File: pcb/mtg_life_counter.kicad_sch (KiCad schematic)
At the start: 41 parts, among them J1 GCT USB-4135-GF-A, J2 ICSP, J3 TP_UART, SW1 MODE SW, SW2 MODE SW, U1 ATmega328P-AU, Y1 16MHz

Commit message: continue layout. update bom
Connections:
- net BTN_RESET: now also U1.13 (PB1); no longer U1.12 (PB0(ICP))
- net BTN_ROLL: now also U1.12 (PB0(ICP)); no longer U1.11 (PD7)
- net LATCH: now also U1.11 (PD7); no longer U1.14 (PB2(CS))
- net MODE_SW: now also U1.14 (PB2(CS)); no longer U1.13 (PB1)
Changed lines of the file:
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@@
 	)
 	(label "LATCH"
-		(at 124.46 50.8 180)
+		(at 124.46 78.74 180)
 		(effects
 			(font
@@
 	)
 	(label "MODE_SW"
-		(at 124.46 53.34 180)
+		(at 124.46 50.8 180)
 		(effects
 			(font
@@
 	)
 	(label "BTN_RESET"
-		(at 124.46 55.88 180)
+		(at 124.46 53.34 180)
 		(effects
 			(font
@@
 	)
 	(label "BTN_ROLL"
-		(at 124.46 78.74 180)
-		(effects
-			(font
+		(at 124.46 55.88 180)
+		(effects
+			(font

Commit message: continue layout. update leds for KD4 led modules
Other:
- note added: "Player 3 Display Bank - Amber"
- note removed: "Player 3 Display Bank - Yellow"
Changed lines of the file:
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@@
 		)
 	)
-	(text "Player 3 Display Bank - Yellow"
+	(text "Player 3 Display Bank - Amber"
 		(exclude_from_sim no)
 		(at 350.52 100.33 0)
@@
 	(wire
 		(pts
-			(xy 100.33 96.52) (xy 124.46 96.52)
+			(xy 100.33 96.52) (xy 132.08 96.52)
 		)
 		(stroke
@@
 		)
 	)
+	(label "RX"
+		(at 132.08 96.52 180)
+		(effects
+			(font
+				(size 1.27 1.27)
+			)
+			(justify right bottom)
+		)
+	)

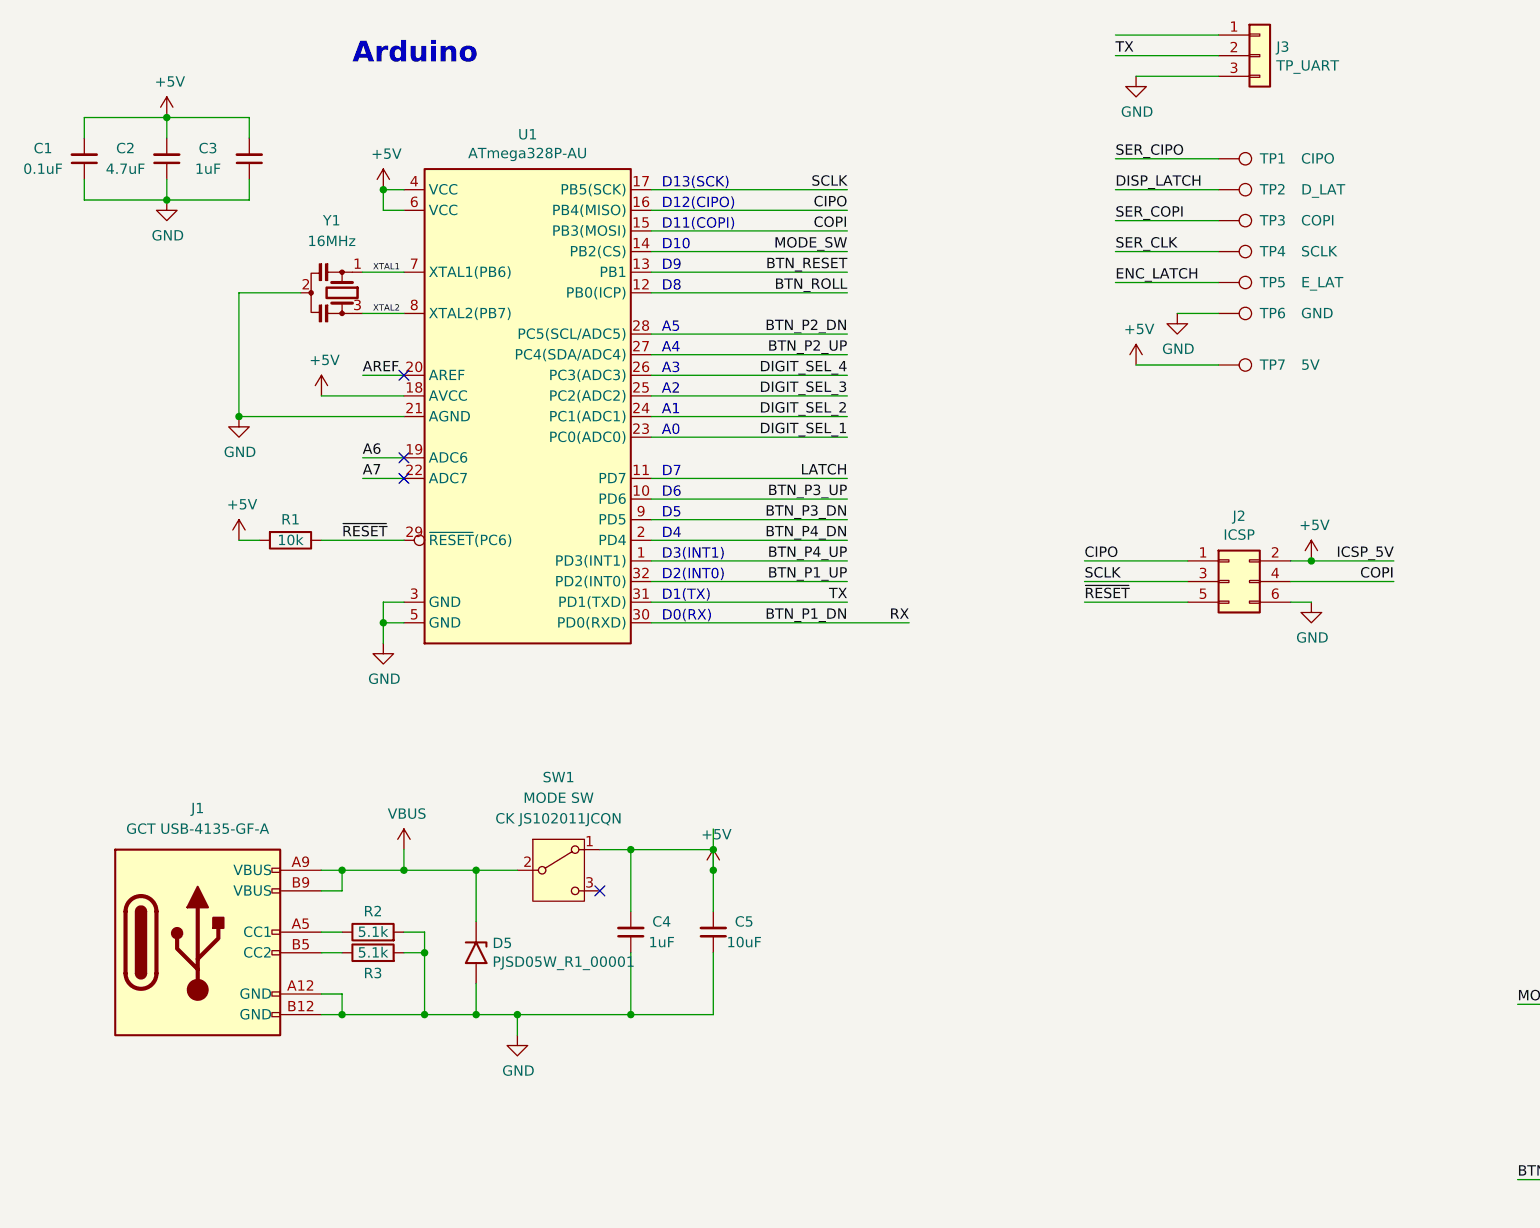
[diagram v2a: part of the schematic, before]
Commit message: complete routing
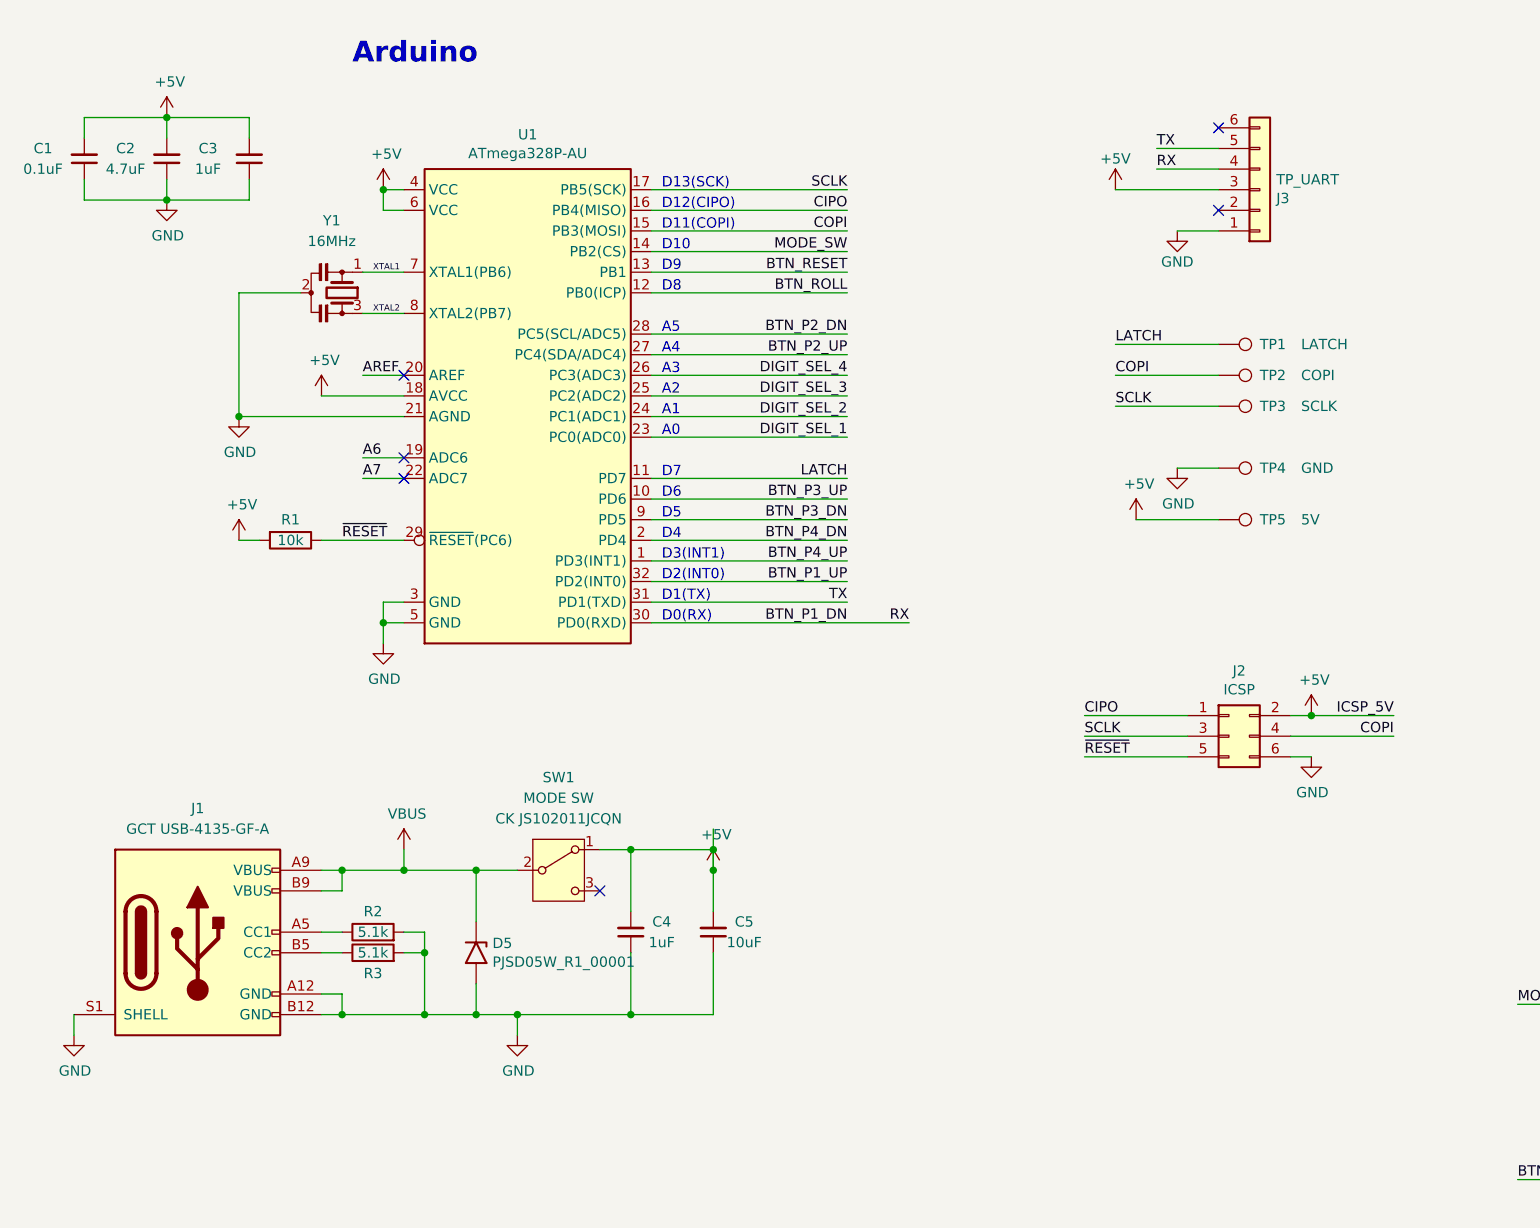
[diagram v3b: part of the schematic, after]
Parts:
- removed TP1: CIPO, TestPoint:TestPoint_Pad_D2.0mm, symbol Connector:TestPoint
- removed TP5: E_LAT, TestPoint:TestPoint_Pad_D2.0mm, symbol Connector:TestPoint
- J3: footprint mtg_life_counter:TP_Edge_3 -> mtg_life_counter:TP_Edge_6; symbol Connector_Generic:Conn_01x03 -> Connector_Generic:Conn_01x06
- TP1: renamed from TP2; value D_LAT -> LATCH; footprint TestPoint:TestPoint_Pad_D2.0mm -> TestPoint:TestPoint_Pad_D1.5mm
- TP2: renamed from TP3; footprint TestPoint:TestPoint_Pad_D2.0mm -> TestPoint:TestPoint_Pad_D1.5mm
- TP3: renamed from TP4; footprint TestPoint:TestPoint_Pad_D2.0mm -> TestPoint:TestPoint_Pad_D1.5mm
- TP4: renamed from TP6; footprint TestPoint:TestPoint_Pad_D2.0mm -> TestPoint:TestPoint_Pad_D1.5mm
- TP5: renamed from TP7; footprint TestPoint:TestPoint_Pad_D2.0mm -> TestPoint:TestPoint_Pad_D1.5mm
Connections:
- net DISP_LATCH is gone; now on net LATCH: TP1.1
- net SER_CLK is gone; now on net SCLK: TP3.1
- net SER_COPI is gone; now on net COPI: TP2.1
- net +5V: now also J3.3 (Pin_3)
- net BTN_P1_DN: now also J3.4 (Pin_4)
- net GND: now also J1.S1 (SHELL), J3.1 (Pin_1); no longer J3.3 (Pin_3)
- net TX: now also J3.5 (Pin_5); no longer J3.2 (Pin_2)
- no-connect marks 6 -> 8
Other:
- moved on the sheet: J2, TP1, TP2, TP3, TP4, TP5
